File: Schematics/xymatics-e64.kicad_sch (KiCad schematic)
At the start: 121 parts, among them J12 STM32 SWD, J13 X-STOP, J14 Y-STOP, J15 Z-STOP, J16 5V POWER, J17 CAN1, J18 CAN2, J19 CAN3, J20 CAN4, J21 CAN5, J22 CAN6, J23 CAN7, J24 CAN8, J25 FAN1, J26 HEATBED, J27 FAN2, J28 FAN3, J29 FAN4, J30 FAN5, J35 BED THERMISTOR, Q1 BED, Q2 FAN1, Q3 FAN2, Q4 FAN3, Q5 FAN4, Q6 FAN5, SW2 STM32 RESET, SW3 STM32 BOOT, U10 STM32F407VET6, U11 MOTOR A, U12 MOTOR B, U13 MOTOR Z1, U14 MOTOR Z2, U15 MOTOR Z3, U16 TPS54302, U17 AMS1117CD-3.3, U18 TJA1051T-3, Y2 16MHZ

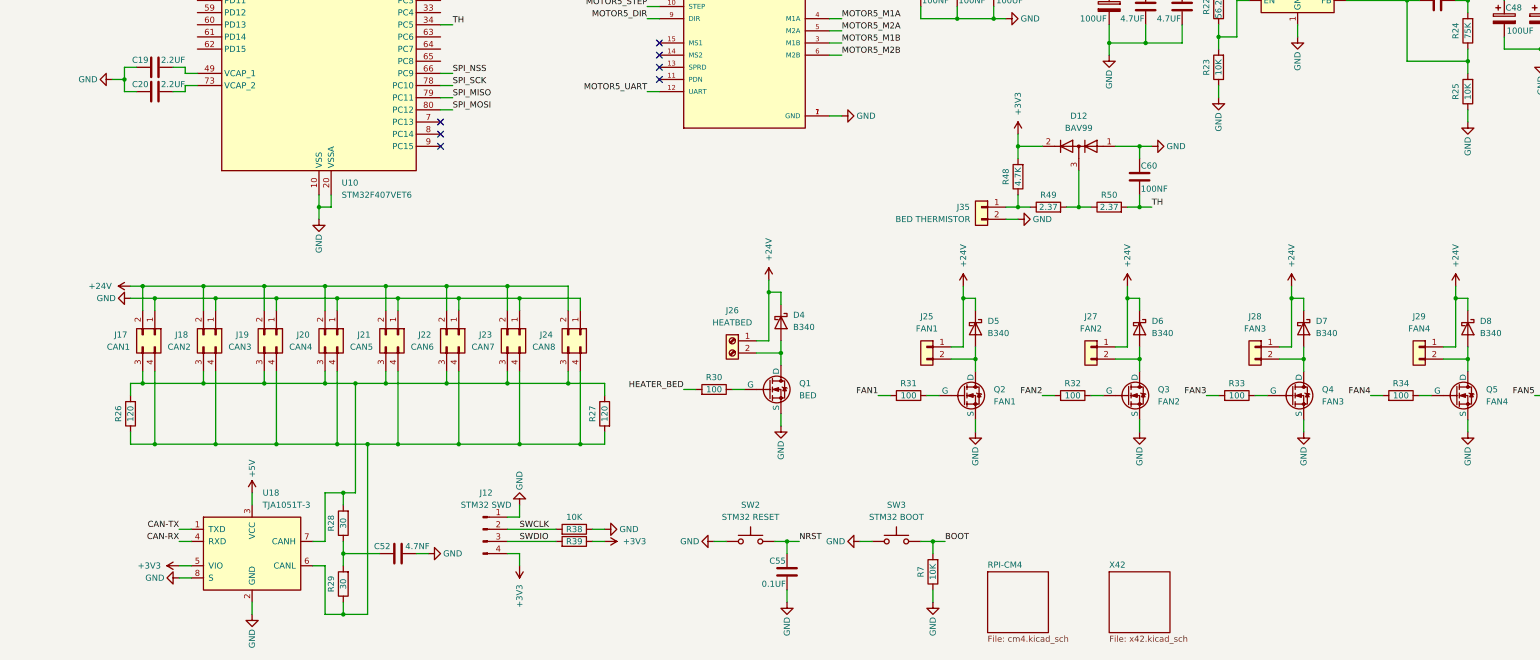
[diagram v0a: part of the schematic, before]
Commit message: Update Schematics
Update CM4, X42, XYmatics-E64 schematics
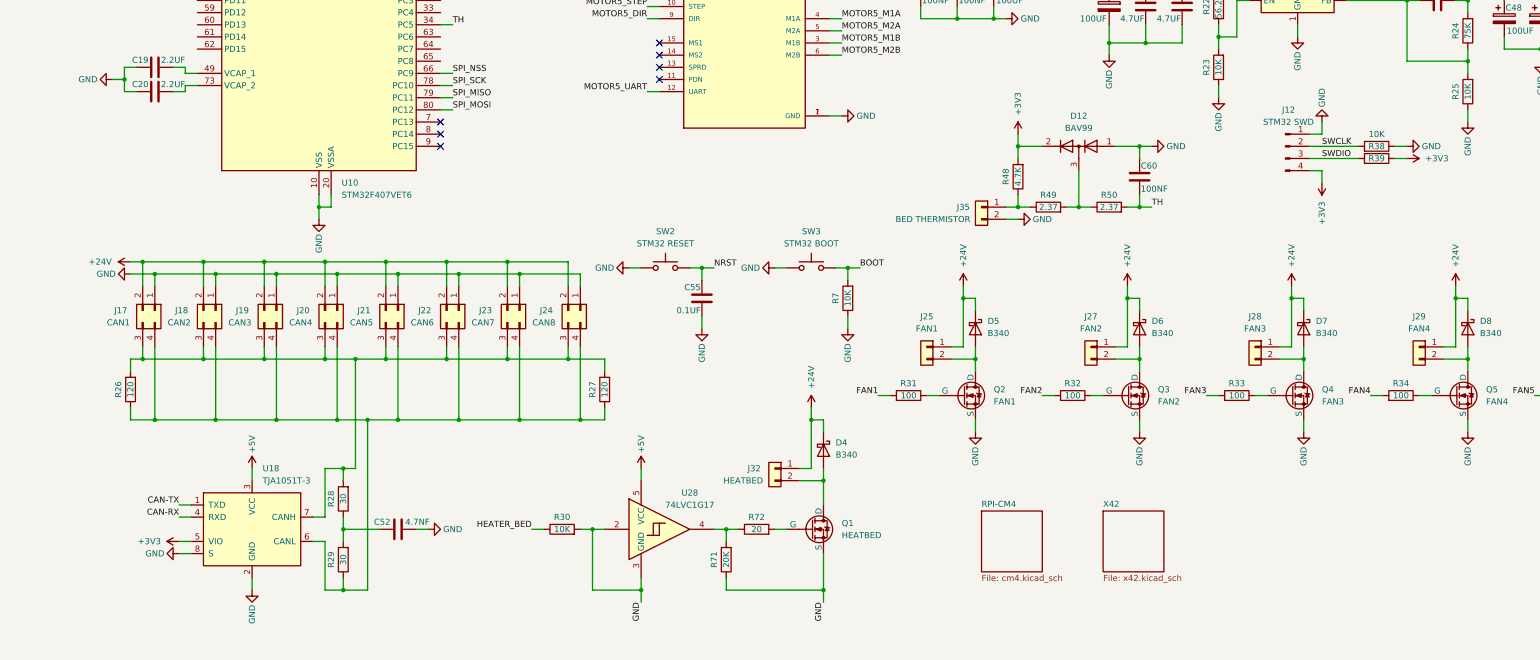
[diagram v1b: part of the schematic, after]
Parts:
- removed J26: HEATBED, symbol Connector:Screw_Terminal_01x02
- added J32: HEATBED, symbol Connector_Generic:Conn_01x02
- added R71: 20K, symbol Device:R
- added R72: 20, symbol Device:R
- added U28: 74LVC1G17, symbol 74xGxx:74LVC1G17
- Q1: value BED -> HEATBED
- R30: value 100 -> 10K
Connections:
- net +24V: now also J32.1 (Pin_1)
- net +5V: now also U28.5 (VCC)
- net GND: now also R30.2, R71.1, U28.2, U28.3 (GND)
- net HEATER_BED: now also R30.1; no longer R30.2
- net at D4.2 (A), Q1.1 (D): now also J32.2 (Pin_2)
- net at Q1.2 (G): now also R72.2; no longer R30.1
- new net: R71.2, R72.1, U28.4
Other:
- company, title: (none) -> XYmatics E64
- moved on the sheet: C52, C55, J12, J17, J18, J19, J20, J21, J22, J23, J24, R26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

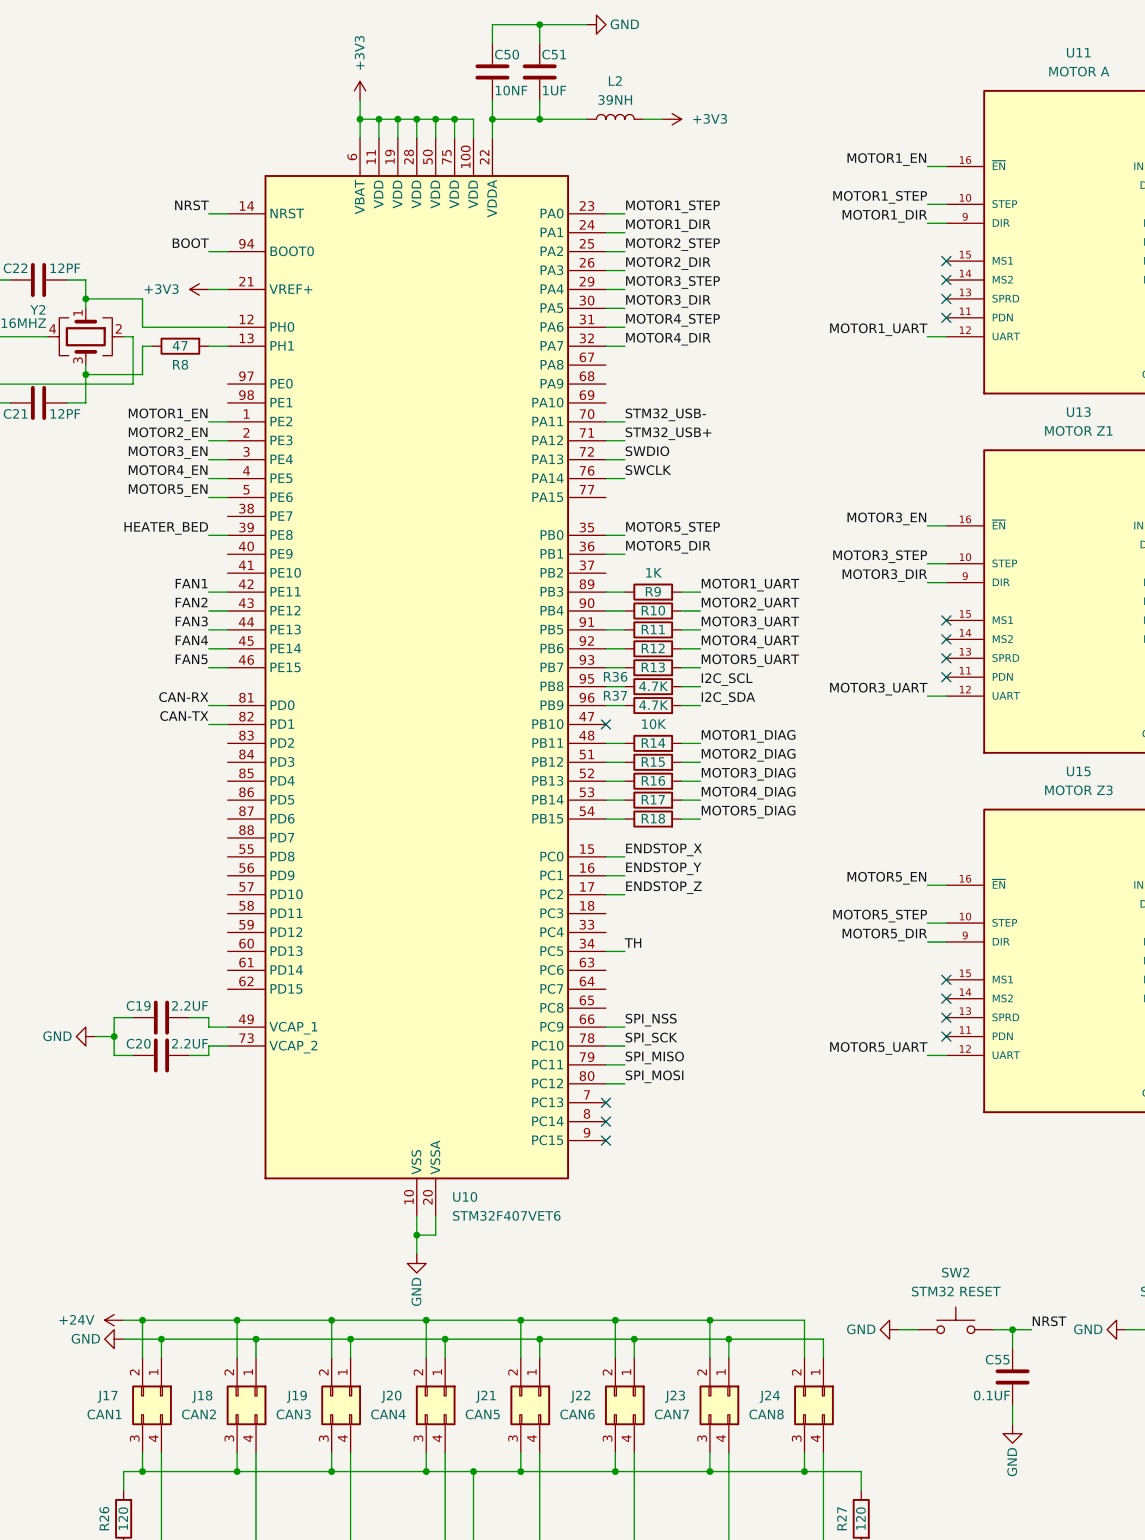
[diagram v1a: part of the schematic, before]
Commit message: Update X42 schematics, Add project PCB
Removed Neopixel and BLTouch breakouts from X42, added X42 PCB (unfinished)
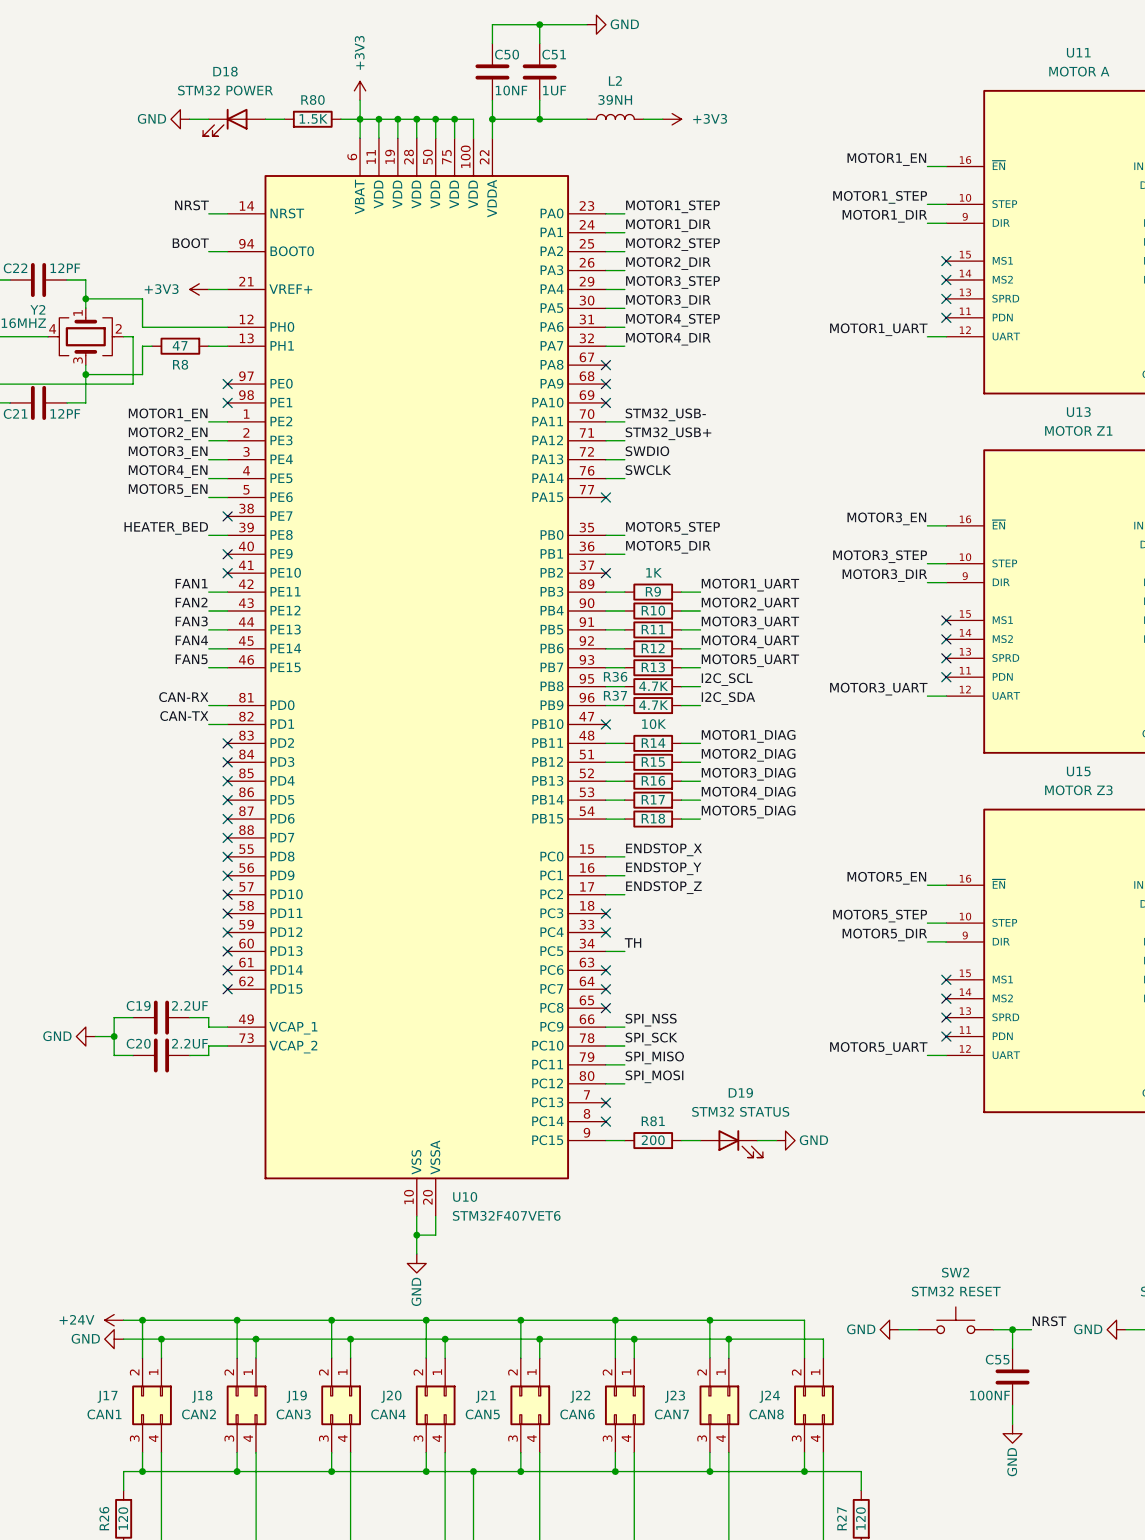
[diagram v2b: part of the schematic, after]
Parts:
- added D18: STM32 POWER, LED_SMD:LED_0805_2012Metric, symbol Device:LED
- added D19: STM32 STATUS, LED_SMD:LED_0805_2012Metric, symbol Device:LED
- added R80: 1.5K, Resistor_SMD:R_0805_2012Metric, symbol Device:R
- added R81: 200, Resistor_SMD:R_0805_2012Metric, symbol Device:R
- C19, C20, C21, C22, C23, C24, C25, C27, C28, C29, C31, C32, C33, C35, C36, C37, C39, C40, C41, C44, C45, C46, C47, C50, C51, C52, C54, C60: footprint (none) -> Capacitor_SMD:C_0805_2012Metric
- C26, C30, C34, C38, C42, C43, C48, C49, C53: footprint (none) -> Capacitor_SMD:CP_Elec_5x3
- C55: value 0.1UF -> 100NF; footprint (none) -> Capacitor_SMD:C_0805_2012Metric
- J12: footprint (none) -> Connector_PinHeader_2.54mm:PinHeader_1x04_P2.54mm_Vertical
- J16: footprint (none) -> Connector_PinHeader_2.54mm:PinHeader_1x03_P2.54mm_Vertical
- J17, J18, J19, J20, J21, J22, J23, J24: footprint Connector_Molex:Molex_Mini-Fit_Jr_5566-04A_2x02_P4.20mm_Vertical -> Connector_Molex:Molex_Micro-Fit_3.0_43045-0412_2x02_P3.00mm_Vertical
- J32, J35: footprint (none) -> Connector_JST:JST_XH_B2B-XH-A_1x02_P2.50mm_Vertical
- L1: footprint (none) -> Inductor_SMD:L_6.3x6.3_H3
- L2: footprint (none) -> Inductor_SMD:L_0805_2012Metric
- Q1: footprint (none) -> Package_TO_SOT_SMD:TO-252-2
- Q2, Q3, Q4, Q5, Q6: footprint (none) -> Package_TO_SOT_SMD:SOT-23
- R10, R11, R12, R13, R14, R15, R16, R17, R18, R19, R20, R21, R23, R24, R25, R26, R27, R28, R29, R30, R31, R32, R33, R34, R35, R36, R37, R38, R39, R48, R49, R50, R7, R71, R72, R8, R9: footprint (none) -> Resistor_SMD:R_0805_2012Metric
- R22: footprint (none) -> Resistor_SMD:R_1206_3216Metric
- SW2, SW3: footprint (none) -> Button_Switch_SMD:SW_Tactile_SPST_NO_Straight_CK_PTS636Sx25SMTRLFS
- U28: footprint (none) -> Package_TO_SOT_SMD:SOT-23-5
- Y2: footprint (none) -> Crystal:Crystal_SMD_Abracon_ABM3B-4Pin_5.0x3.2mm
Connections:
- net +3V3: now also R80.1
- net GND: now also D18.1 (K), D19.1 (K)
- net at U10.9 (PC15): now also R81.1
- new net: D19.2 (A), R81.2
- new net: D18.2 (A), R80.2
- no-connect marks 29 -> 57
